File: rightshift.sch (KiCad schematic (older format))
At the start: 15 parts

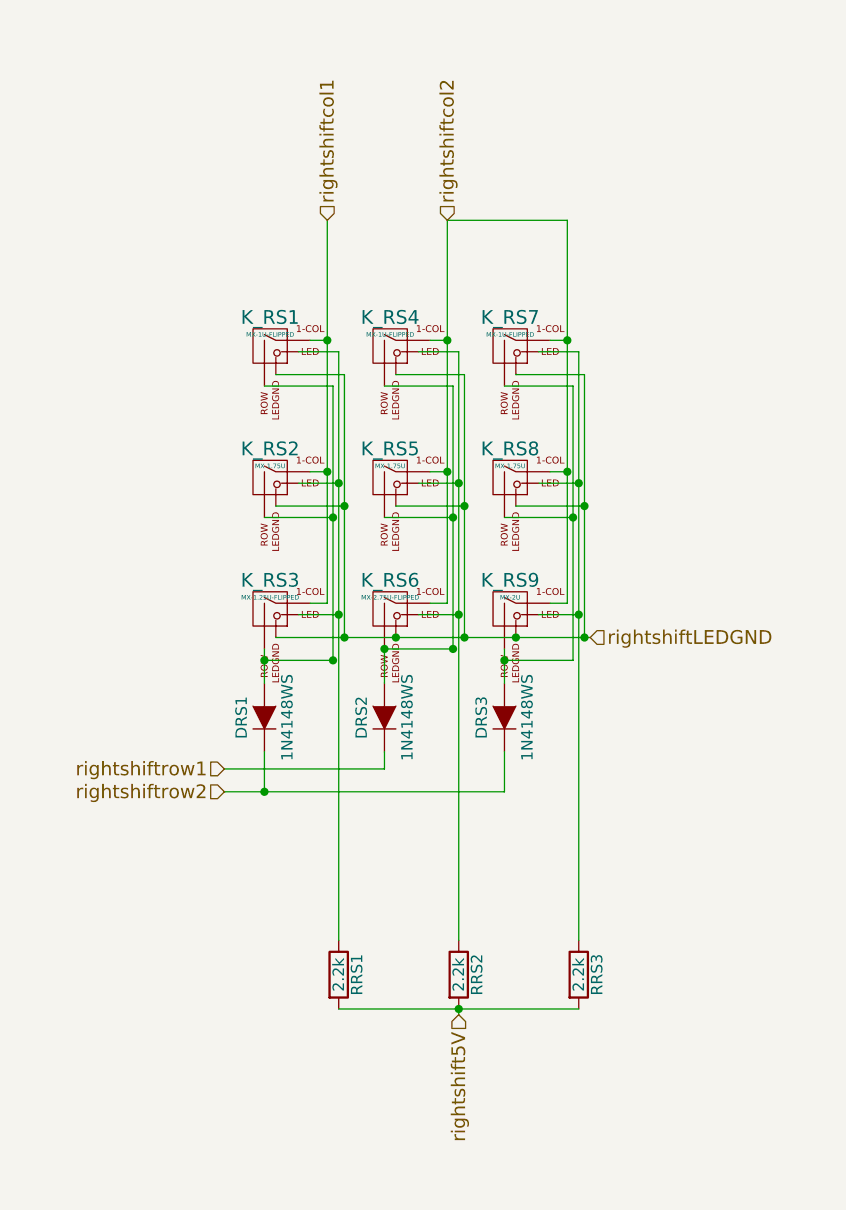
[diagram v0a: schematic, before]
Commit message: Added new right shift layout and rotated ISO stabs
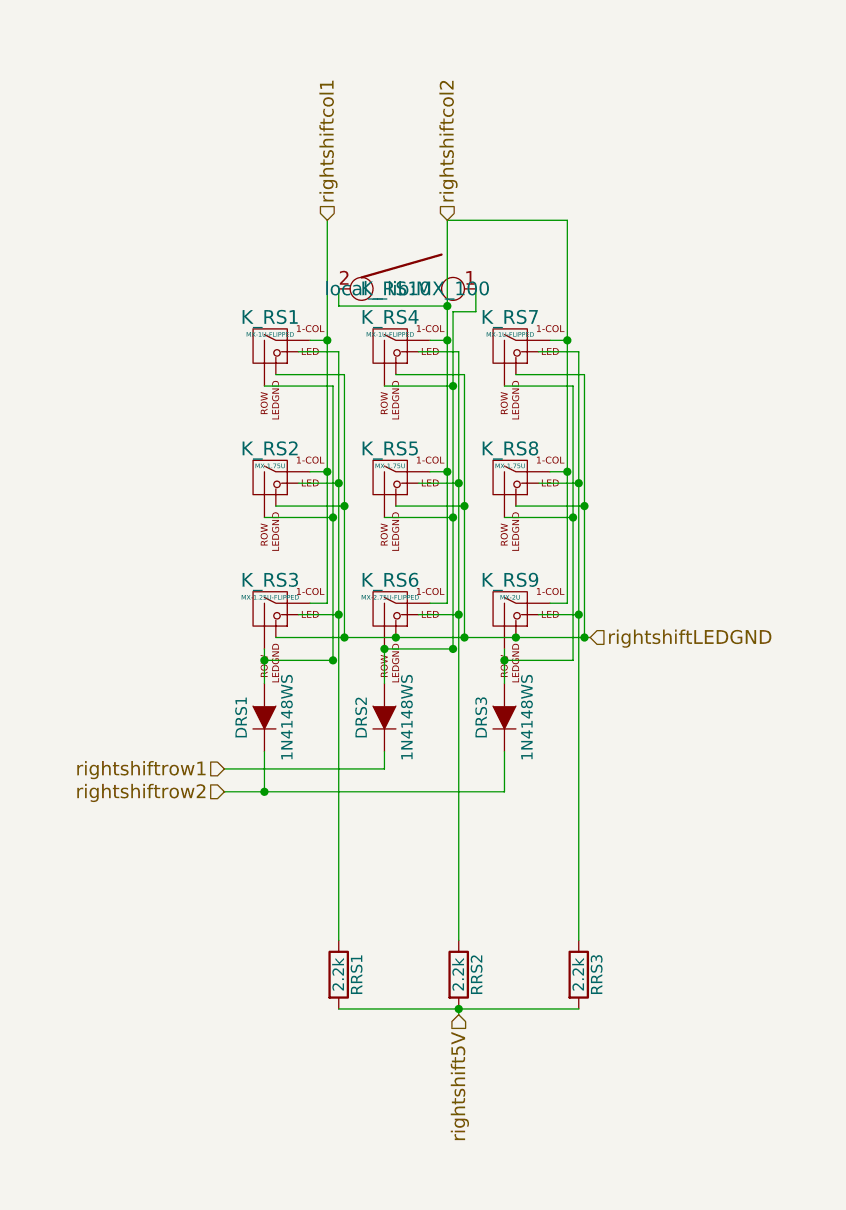
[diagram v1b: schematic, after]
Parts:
- added K_RS10: KEYSW, local__lib:MX_100, symbol KEYSW
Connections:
- net rightshiftcol2: now also K_RS10.2
- net at DRS2.2 (A), K_RS4.1 (ROW), K_RS5.2 (ROW)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: now also K_RS10.1
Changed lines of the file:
@@
 	5300 2425 5600 2425
 Wire Wire Line
-	5600 2425 5600 3575
+	5600 2100 5600 3575
 Wire Wire Line
 	5600 3000 5300 3000
@@
 	1    0    0    -1
 $EndComp
+$Comp
+L KEYSW K_RS10
+U 1 1 599058B9
+P 5400 2000
+F 0 "K_RS10" H 5350 2000 60  0000 C CNN
+F 1 "KEYSW" H 5400 1900 60  0001 C CNN
+F 2 "local__lib:MX_100" H 5400 2000 60  0000 C CNN
+F 3 "" H 5400 2000 60  0000 C CNN
+	1    5400 2000
+	1    0    0    -1
+$EndComp
+Wire Wire Line
+	5575 2075 5100 2075
+Wire Wire Line
+	5100 2075 5100 2000
+Connection ~ 5575 2075
+Wire Wire Line
+	5600 2100 5700 2100
+Wire Wire Line
+	5700 2100 5700 2000
+Connection ~ 5600 2425
 $EndSCHEMATC
